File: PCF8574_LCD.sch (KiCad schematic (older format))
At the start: 11 parts, among them P1 CONN_4, U1 PCF8574

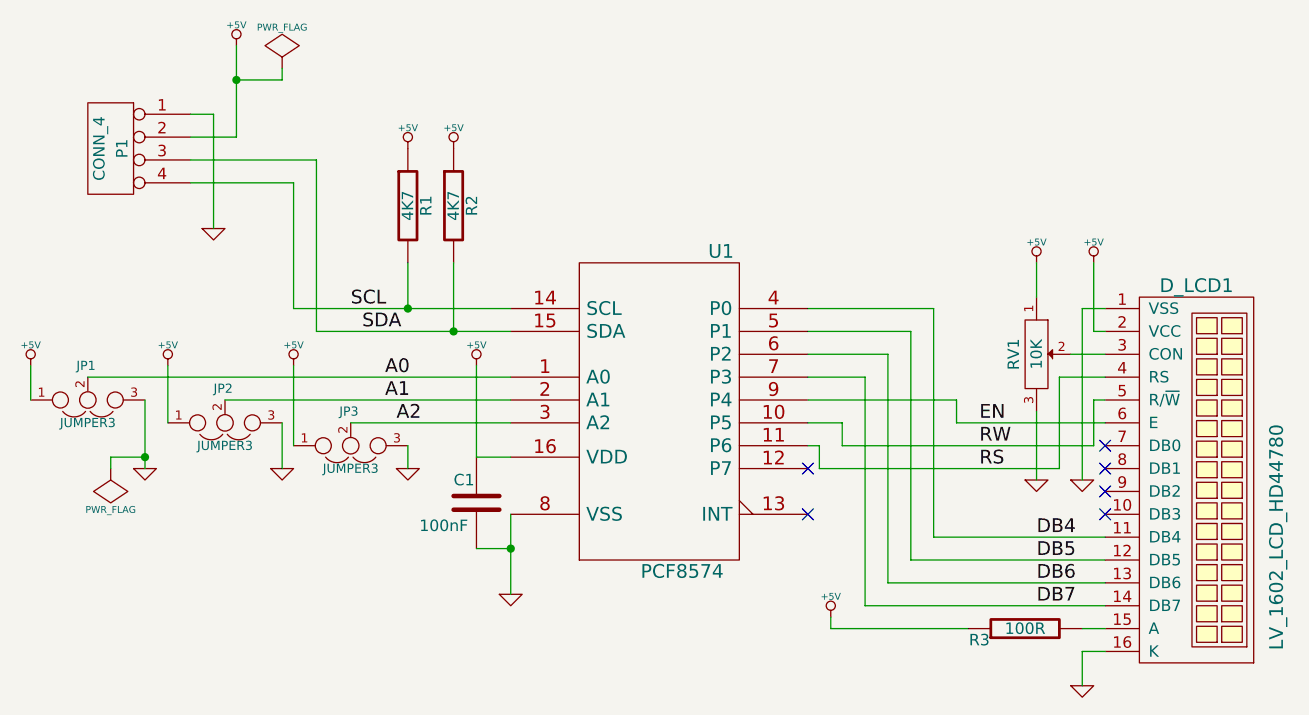
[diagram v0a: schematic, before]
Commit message: v.0.2: Single, through-hole address jumper
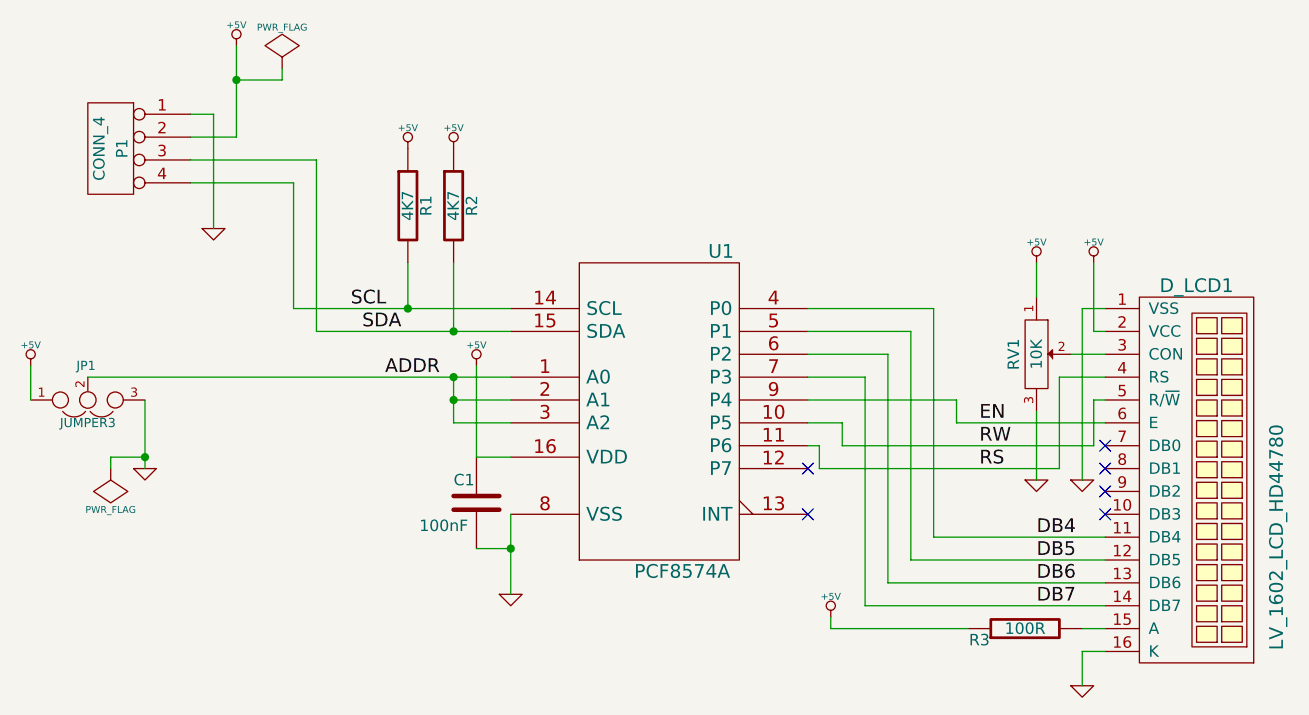
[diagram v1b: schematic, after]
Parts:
- removed JP2, JP3: JUMPER3, symbol JUMPER3
- U1: value PCF8574 -> PCF8574A
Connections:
- net A1 is gone; now on net ADDR: U1.2 (A1)
- net A2 is gone; now on net ADDR: U1.3 (A2)
- net A0 renamed ADDR
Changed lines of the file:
@@
 Sheet 1 1
 Title "I2C expansion for a HD44780-compatible 16x02 LCD"
-Date "29 feb 2012"
+Date "14 jul 2012"
 Rev "0.1"
 Comp "Released under the Creative Commons Attribution Share-Alike 3.0"
@@
 Wire Wire Line
 	2000 3100 3850 3100
-Wire Wire Line
-	2900 3050 2900 3400
-Wire Wire Line
-	2850 3300 2850 3500
-Wire Wire Line
-	3400 3400 3400 3500
 Connection ~ 3400 2800
 Wire Wire Line
@@
 Wire Wire Line
 	3700 3450 3850 3450
-Wire Wire Line
-	3150 3300 3850 3300
-Wire Wire Line
-	2600 3200 3850 3200
-Wire Wire Line
-	2350 3050 2350 3300
 Wire Wire Line
 	2250 3200 2250 3500
@@
 	0    1    1    0
 $EndComp
-Text Label 3350 3300 0    60   ~ 0
-A2
-Text Label 3300 3200 0    60   ~ 0
-A1
 Text Label 3300 3100 0    60   ~ 0
-A0
+ADDR
 $Comp
 L GND #PWR05
@@
 $EndComp
 $Comp
-L GND #PWR08
-U 1 1 4F4549F2
-P 2850 3500
-F 0 "#PWR08" H 2850 3500 30  0001 C CNN
-F 1 "GND" H 2850 3430 30  0001 C CNN
-	1    2850 3500
-	1    0    0    -1
-$EndComp
-$Comp
 L +5V #PWR09
 U 1 1 4F4549EF
@@
 F 1 "+5V" H 1750 3140 30  0000 C CNN
 	1    1750 3050
-	1    0    0    -1
-$EndComp
-$Comp
-L +5V #PWR010
-U 1 1 4F4549EB
-P 2350 3050
-F 0 "#PWR010" H 2350 3140 20  0001 C CNN
-F 1 "+5V" H 2350 3140 30  0000 C CNN
-	1    2350 3050
-	1    0    0    -1
-$EndComp
-$Comp
-L +5V #PWR011
-U 1 1 4F4549D1
-P 2900 3050
-F 0 "#PWR011" H 2900 3140 20  0001 C CNN
-F 1 "+5V" H 2900 3140 30  0000 C CNN
-	1    2900 3050
-	1    0    0    -1
-$EndComp
-$Comp
-L GND #PWR012
-U 1 1 4F4549CD
-P 3400 3500
-F 0 "#PWR012" H 3400 3500 30  0001 C CNN
-F 1 "GND" H 3400 3430 30  0001 C CNN
-	1    3400 3500
 	1    0    0    -1
 $EndComp
@@
 $EndComp
 $Comp
-L JUMPER3 JP2
-U 1 1 4F4547F1
-P 2600 3300
-F 0 "JP2" H 2550 3150 40  0000 L CNN
-F 1 "JUMPER3" H 2600 3400 40  0000 C CNN
-	1    2600 3300
-	1    0    0    1
-$EndComp
-$Comp
-L JUMPER3 JP3
-U 1 1 4F4547EB
-P 3150 3400
-F 0 "JP3" H 3100 3250 40  0000 L CNN
-F 1 "JUMPER3" H 3150 3500 40  0000 C CNN
-	1    3150 3400
-	1    0    0    1
-$EndComp
-$Comp
 L JUMPER3 JP1
 U 1 1 4F4547D3
@@
 P 4500 3250
 F 0 "U1" H 4770 3950 60  0000 C CNN
-F 1 "PCF8574" H 4600 2550 60  0000 C CNN
+F 1 "PCF8574A" H 4600 2550 60  0000 C CNN
 	1    4500 3250
 	1    0    0    -1
 $EndComp
+Wire Wire Line
+	3600 3100 3600 3300
+Wire Wire Line
+	3600 3300 3850 3300
+Connection ~ 3600 3100
+Wire Wire Line
+	3850 3200 3600 3200
+Connection ~ 3600 3200
 $EndSCHEMATC

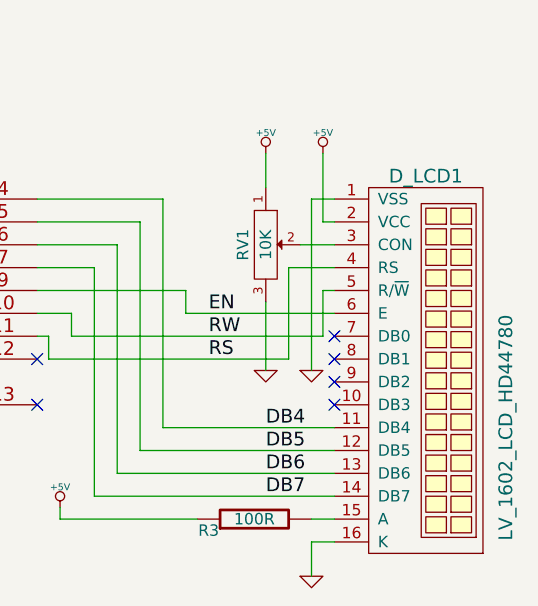
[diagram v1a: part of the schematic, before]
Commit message: v.0.3: Larger pads, 20mil traces
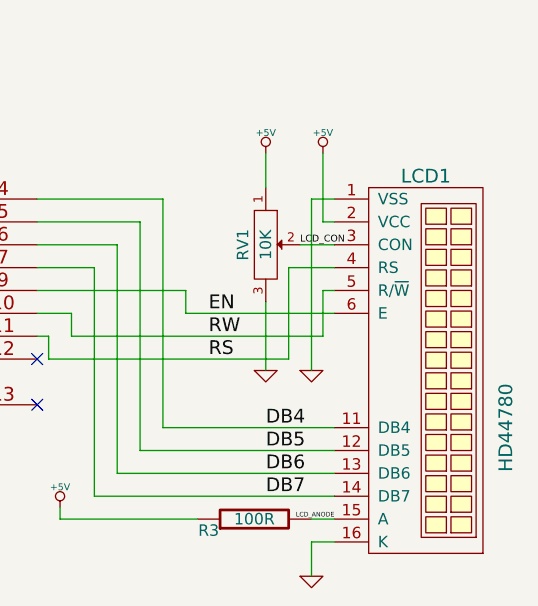
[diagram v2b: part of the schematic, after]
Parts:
- removed D_LCD1: LV_1602_LCD_HD44780, symbol LV_1602_LCD_HD44780
- added LCD1: HD44780, symbol LV_1602_LCD_HD44780_6+6
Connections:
- net +5V: now also LCD1.2 (VCC)
- net DB4: now also LCD1.11 (DB4)
- net DB5: now also LCD1.12 (DB5)
- net DB6: now also LCD1.13 (DB6)
- net DB7: now also LCD1.14 (DB7)
- net EN: now also LCD1.6 (E)
- net GND: now also LCD1.1 (VSS), LCD1.16 (K)
- net RS: now also LCD1.4 (RS)
- net RW: now also LCD1.5 (R/~W)
- net LCD_ANODE: now reaches R3.2
- net LCD_ANODE: now also LCD1.15 (A)
- net LCD_CON: now reaches RV1.2
- net LCD_CON: now also LCD1.3 (CON)
- no-connect marks 6 -> 2
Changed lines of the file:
@@
-EESchema Schematic File Version 2  date 29/02/2012 08:42:45
+EESchema Schematic File Version 2  date Sun 01 Jan 2012 00:00:00 AM EEST
 LIBS:power
 LIBS:device
@@
 Sheet 1 1
 Title "I2C expansion for a HD44780-compatible 16x02 LCD"
-Date "14 jul 2012"
-Rev "0.1"
+Date "23 jul 2012"
+Rev "0.3"
 Comp "Released under the Creative Commons Attribution Share-Alike 3.0"
 Comment1 "http://lowvoltage.wordpress.com"
@@
 	-1   0    0    1
 $EndComp
-NoConn ~ 6450 3700
-NoConn ~ 6450 3600
-NoConn ~ 6450 3500
-NoConn ~ 6450 3400
-$Comp
-L LV_1602_LCD_HD44780 D_LCD1
-U 1 1 4F469210
-P 6800 3550
-F 0 "D_LCD1" V 7650 3600 60  0000 C CNN
-F 1 "LV_1602_LCD_HD44780" H 6550 3950 60  0000 C CNN
-	1    6800 3550
-	0    1    -1   0
-$EndComp
 Text Label 3150 2800 0    60   ~ 0
 SCL
@@
 $EndComp
 $Comp
-L +5V #PWR09
+L +5V #PWR08
 U 1 1 4F4549EF
 P 1750 3050
-F 0 "#PWR09" H 1750 3140 20  0001 C CNN
+F 0 "#PWR08" H 1750 3140 20  0001 C CNN
 F 1 "+5V" H 1750 3140 30  0000 C CNN
 	1    1750 3050
@@
 $EndComp
 $Comp
-L +5V #PWR013
+L +5V #PWR09
 U 1 1 4F454988
 P 5250 4150
-F 0 "#PWR013" H 5250 4240 20  0001 C CNN
+F 0 "#PWR09" H 5250 4240 20  0001 C CNN
 F 1 "+5V" H 5250 4240 30  0000 C CNN
 	1    5250 4150
@@
 $EndComp
 $Comp
-L +5V #PWR014
+L +5V #PWR010
 U 1 1 4F454908
 P 3600 2100
-F 0 "#PWR014" H 3600 2190 20  0001 C CNN
+F 0 "#PWR010" H 3600 2190 20  0001 C CNN
 F 1 "+5V" H 3600 2190 30  0000 C CNN
 	1    3600 2100
@@
 $EndComp
 $Comp
-L +5V #PWR015
+L +5V #PWR011
 U 1 1 4F454906
 P 3400 2100
-F 0 "#PWR015" H 3400 2190 20  0001 C CNN
+F 0 "#PWR011" H 3400 2190 20  0001 C CNN
 F 1 "+5V" H 3400 2190 30  0000 C CNN
 	1    3400 2100
@@
 $EndComp
 $Comp
-L GND #PWR016
+L GND #PWR012
 U 1 1 4F4548DC
 P 2550 2450
-F 0 "#PWR016" H 2550 2450 30  0001 C CNN
+F 0 "#PWR012" H 2550 2450 30  0001 C CNN
 F 1 "GND" H 2550 2380 30  0001 C CNN
 	1    2550 2450
@@
 $EndComp
 $Comp
-L +5V #PWR017
+L +5V #PWR013
 U 1 1 4F4548D9
 P 2650 1650
-F 0 "#PWR017" H 2650 1740 20  0001 C CNN
+F 0 "#PWR013" H 2650 1740 20  0001 C CNN
 F 1 "+5V" H 2650 1740 30  0000 C CNN
 	1    2650 1650
@@
 $EndComp
 $Comp
-L +5V #PWR018
+L +5V #PWR014
 U 1 1 4F4548BE
 P 3700 3050
-F 0 "#PWR018" H 3700 3140 20  0001 C CNN
+F 0 "#PWR014" H 3700 3140 20  0001 C CNN
 F 1 "+5V" H 3700 3140 30  0000 C CNN
 	1    3700 3050
@@
 $EndComp
 $Comp
-L GND #PWR019
+L GND #PWR015
 U 1 1 4F454830
 P 6350 4450
-F 0 "#PWR019" H 6350 4450 30  0001 C CNN
+F 0 "#PWR015" H 6350 4450 30  0001 C CNN
 F 1 "GND" H 6350 4380 30  0001 C CNN
 	1    6350 4450
@@
 $EndComp
 $Comp
-L GND #PWR020
+L GND #PWR016
 U 1 1 4F454828
 P 3850 4050
-F 0 "#PWR020" H 3850 4050 30  0001 C CNN
+F 0 "#PWR016" H 3850 4050 30  0001 C CNN
 F 1 "GND" H 3850 3980 30  0001 C CNN
 	1    3850 4050
@@
 	3850 3200 3600 3200
 Connection ~ 3600 3200
+$Comp
+L LV_1602_LCD_HD44780_6+6 LCD1
+U 1 1 500DA1A2
+P 6800 3550
+F 0 "LCD1" V 7650 3600 60  0000 C CNN
+F 1 "HD44780" H 6550 3950 60  0000 C CNN
+	1    6800 3550
+	0    1    -1   0
+$EndComp
+Text Label 6300 3000 0    30   ~ 0
+LCD_CON
+Text Label 6450 4200 2    20   ~ 0
+LCD_ANODE
 $EndSCHEMATC
